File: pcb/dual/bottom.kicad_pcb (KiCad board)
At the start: 2 copper layers, 242.5 x 87.9 mm, 8 parts

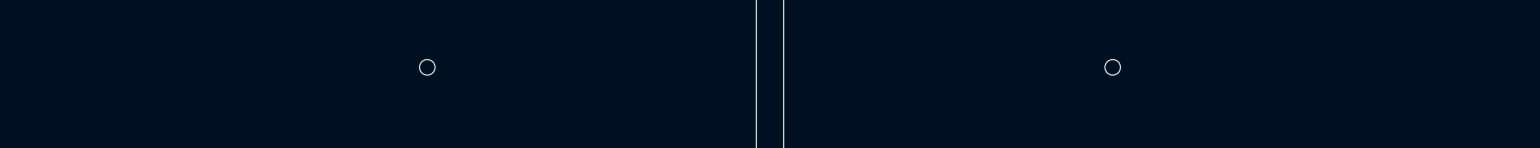
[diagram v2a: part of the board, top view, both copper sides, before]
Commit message: Five standoffs per half, logo on the board, plain controller corner
The standoff the outer pinky column lost moves to where the pinky and ring
columns meet, so the outer top corner is supported again (10 in all). The
logo is back on the board's silkscreen. The jack, reset button and OLED
header lose their printed outlines. The plate's opening by the controller
now starts at the inner index keycap line instead of the stock plate's
fixed edge, clearing the moved controller's sockets by 1.66 mm. The board
records its ENIG finish; renders can hide the jack and reset ("wireless").
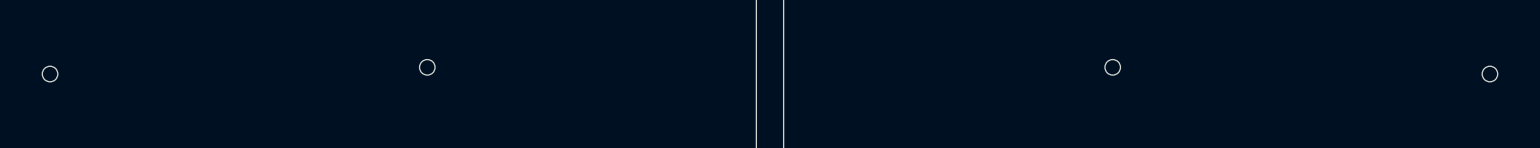
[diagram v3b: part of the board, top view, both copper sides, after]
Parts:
- added H10: , , F.Cu at (186.0, 113.7)
- added H9: , , F.Cu at (231.8, 111.2)
- moved H3 149.1 mm to (65.5, 126.0)
- moved H7 130.5 mm to (107.3, 72.0)
- moved H4 89.1 mm to (204.5, 72.0)
- moved H8 61.5 mm to (246.2, 126.0)
- moved H6 54.3 mm to (258.0, 73.0)
- moved H1 46.3 mm to (53.8, 73.0)
- moved H5 45.6 mm to (125.7, 113.7)
- moved H2 20.7 mm to (79.9, 111.2)

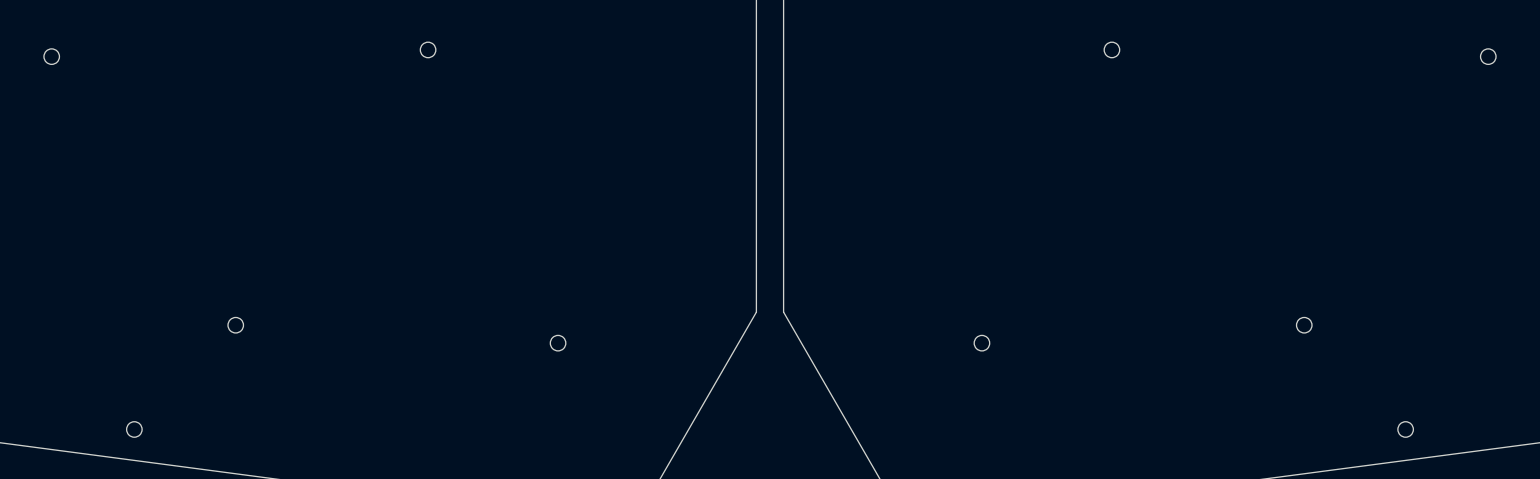
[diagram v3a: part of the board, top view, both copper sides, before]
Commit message: Standoffs placed by geometry
Each standoff between four keys sits at the four keys' centre (midway
between the columns and between their staggered row gaps): pinky and
ring top and bottom, index and inner index at the top. The thumb one
is equally far from its three keycap corners, and the one by the
trackpoint sits at the centre of the key cell the logo's notch outlines.
D29 moves 0.3 mm to make room and stays clear. Standoffs keep 1.5 mm
from the logo.
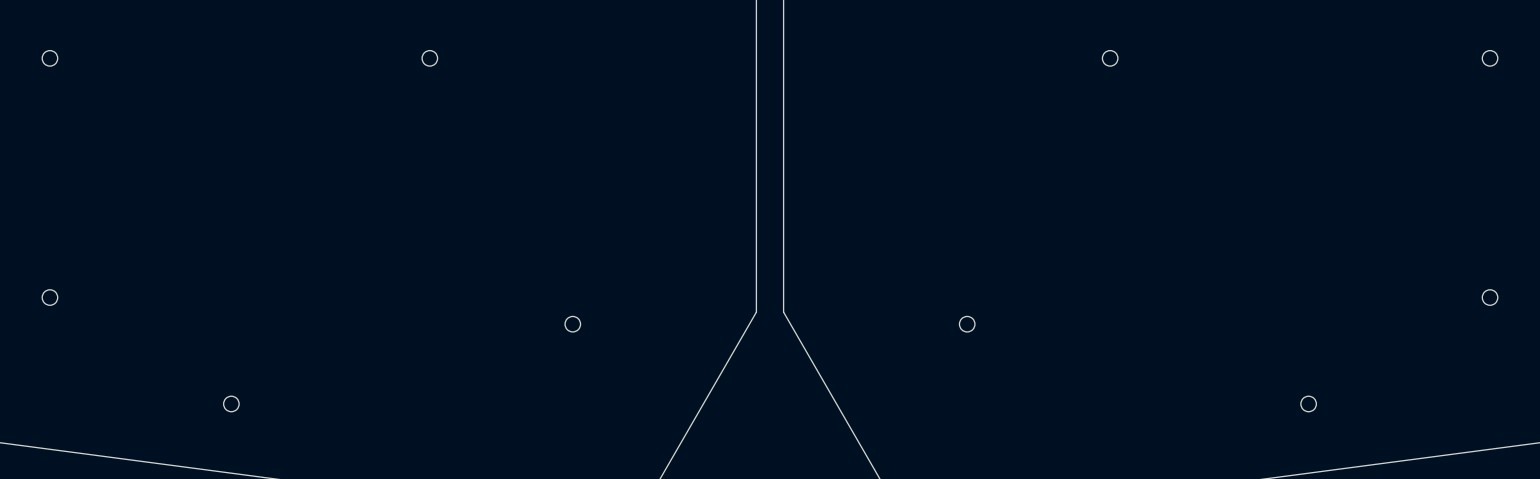
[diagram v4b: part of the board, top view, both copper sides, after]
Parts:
- moved H3 22.3 mm to (53.5, 107.2)
- moved H8 22.3 mm to (258.2, 107.2)
- moved H2 11.2 mm to (79.3, 122.4)
- moved H9 11.2 mm to (232.4, 122.4)
- moved H10 3.41 mm to (183.9, 111.0)
- moved H5 3.41 mm to (127.8, 111.0)
- moved H4 1.22 mm to (204.2, 73.2)
- moved H7 1.22 mm to (107.5, 73.2)
- moved H1 0.35 mm to (53.5, 73.2)
- moved H6 0.35 mm to (258.2, 73.2)
